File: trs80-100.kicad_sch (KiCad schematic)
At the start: 364 parts, among them CN2 A-7224, CN3 TCS-4480, CN4 TCS-4490, CN5 PRINTER CONNECTOR, CN6 RS232C, CN7 LCD-CONN, CN8 LCD-LED-CONN, J1 Adapter Jack CN9, K1 Key_Board, M1 40H373, M10 SystemBus, M11 ROM32k, M12 ROM32k, M13 40H032, M14 40H175, M15 40H244, M16 40H138, M17 40H000, M18 μPD1990AC, M19 80C85, M2 40H245, M20 40H367, M21 40H244, M22 IM6402, M23 40H244, M24 40H032, M25 81C55, M26 40H002, M27 4011, M28 4013, M29 TL064, M3 40H138, M30 TL064, M31 MC14412, M32 40H244, M33 40H157, M34 4584, M35 4584, M36 4013, M4 40H138, M5 40H139, M6 OPTION RAM #3, M7 OPTION RAM #2, M8 OPTION RAM #1, M9 STANDARD RAM, SW3 SLB-22BP-03, SW4 Reset Switch, SW5 SSP32201, T1 2SA1115, T10 2SC2603, T11 2SC2603, T13 2SC2603, T14 2SC2603(E), T15 2SC2603(E), T16 2SC2603(E), T17 2SC2603(E), T18 2SC2603, T19 2SA1115, T2 2SC2603, T20 2SC2603, T21 2SC2603(E), T22 2SC2603(E), T23 2SC2603, T24 2SC2603, T25 2SC2603, T27 2SC2603, T28 2SA1115, T3 2SC2603, T5 2SC2603, T6 2SC2603, T7 2SC2603, T8 2SC2603, T9 2SC2603, X1 32.768kHz, X2 4.9152MHz, X3 1.0MHz

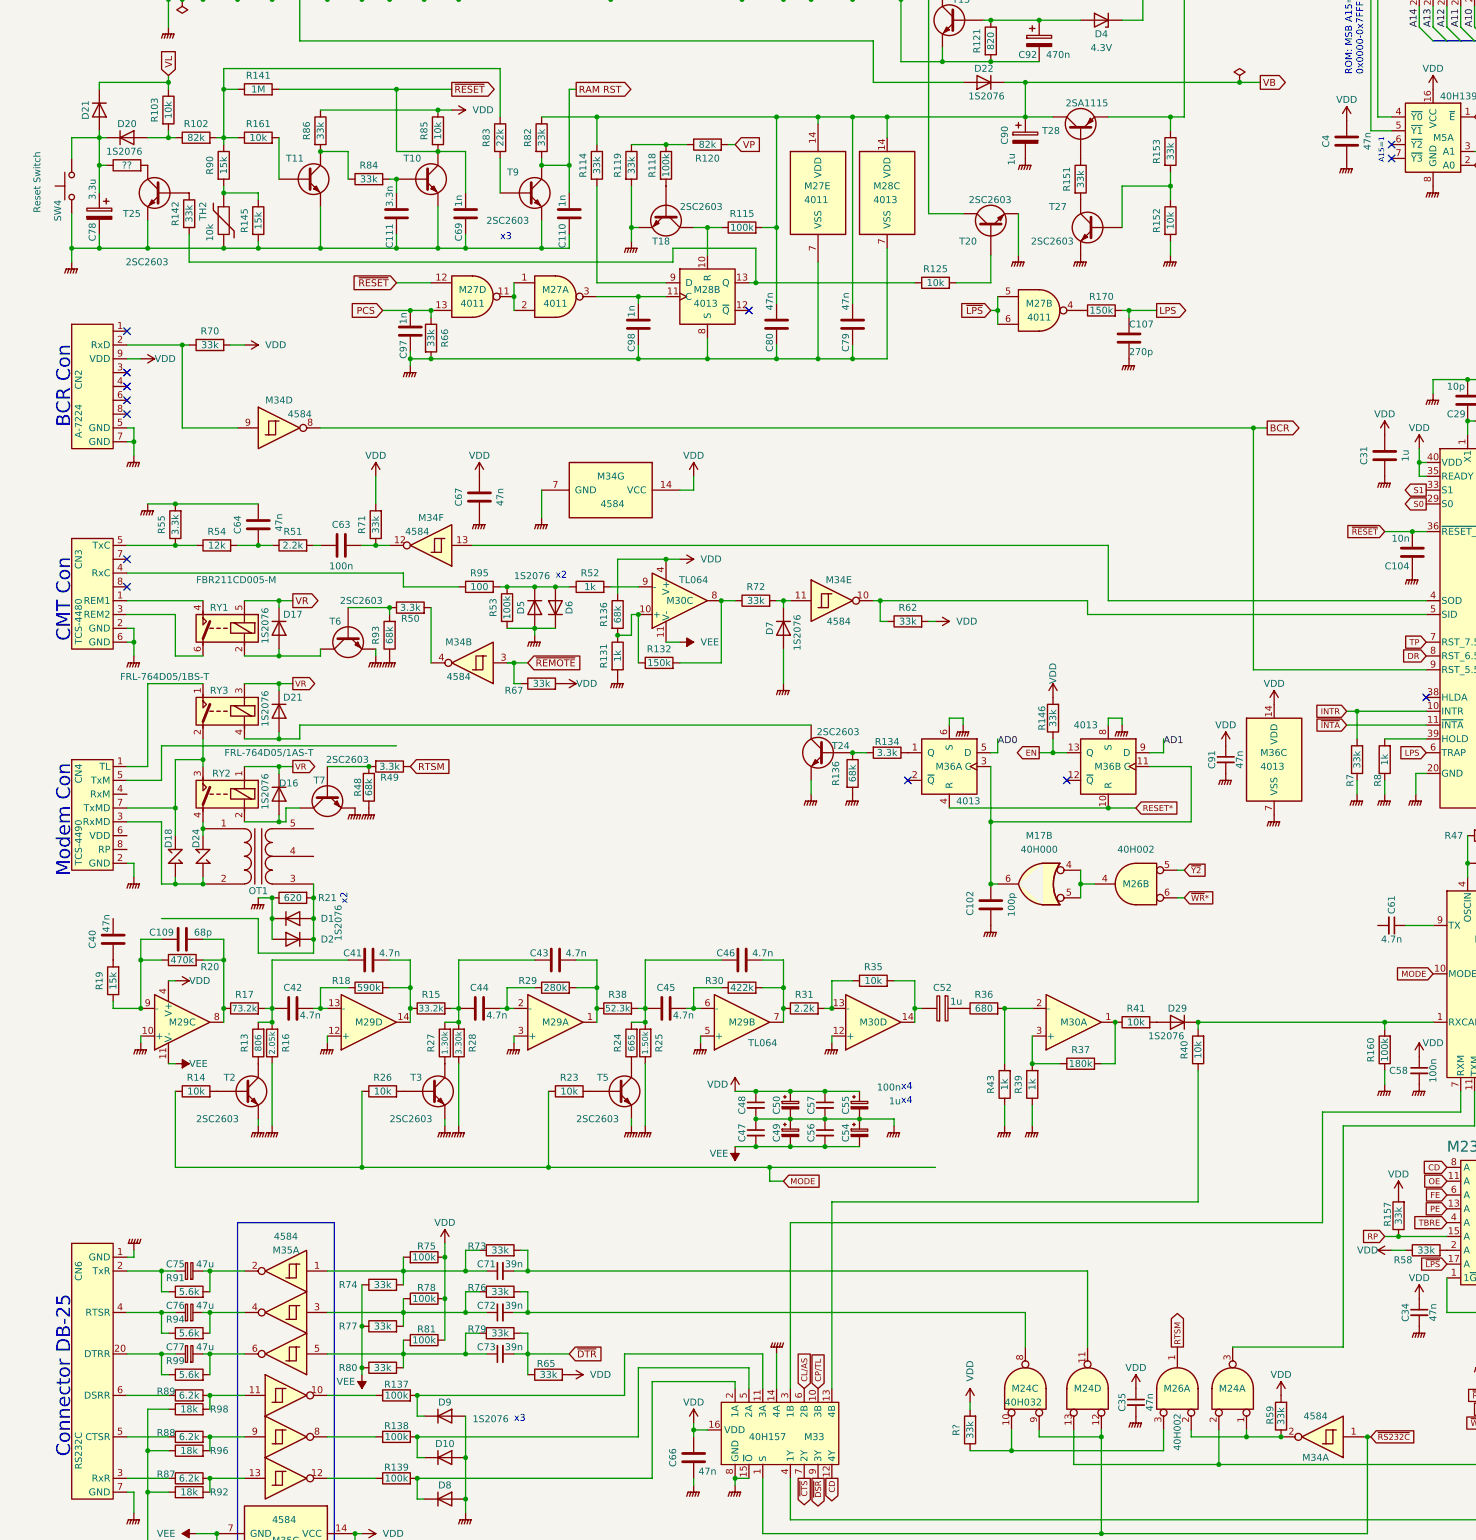
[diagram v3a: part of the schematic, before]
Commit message: Finish modem section.
Initial draft complete. One ERC warning about ~RTS never
used left.
Ready for proof-reading.
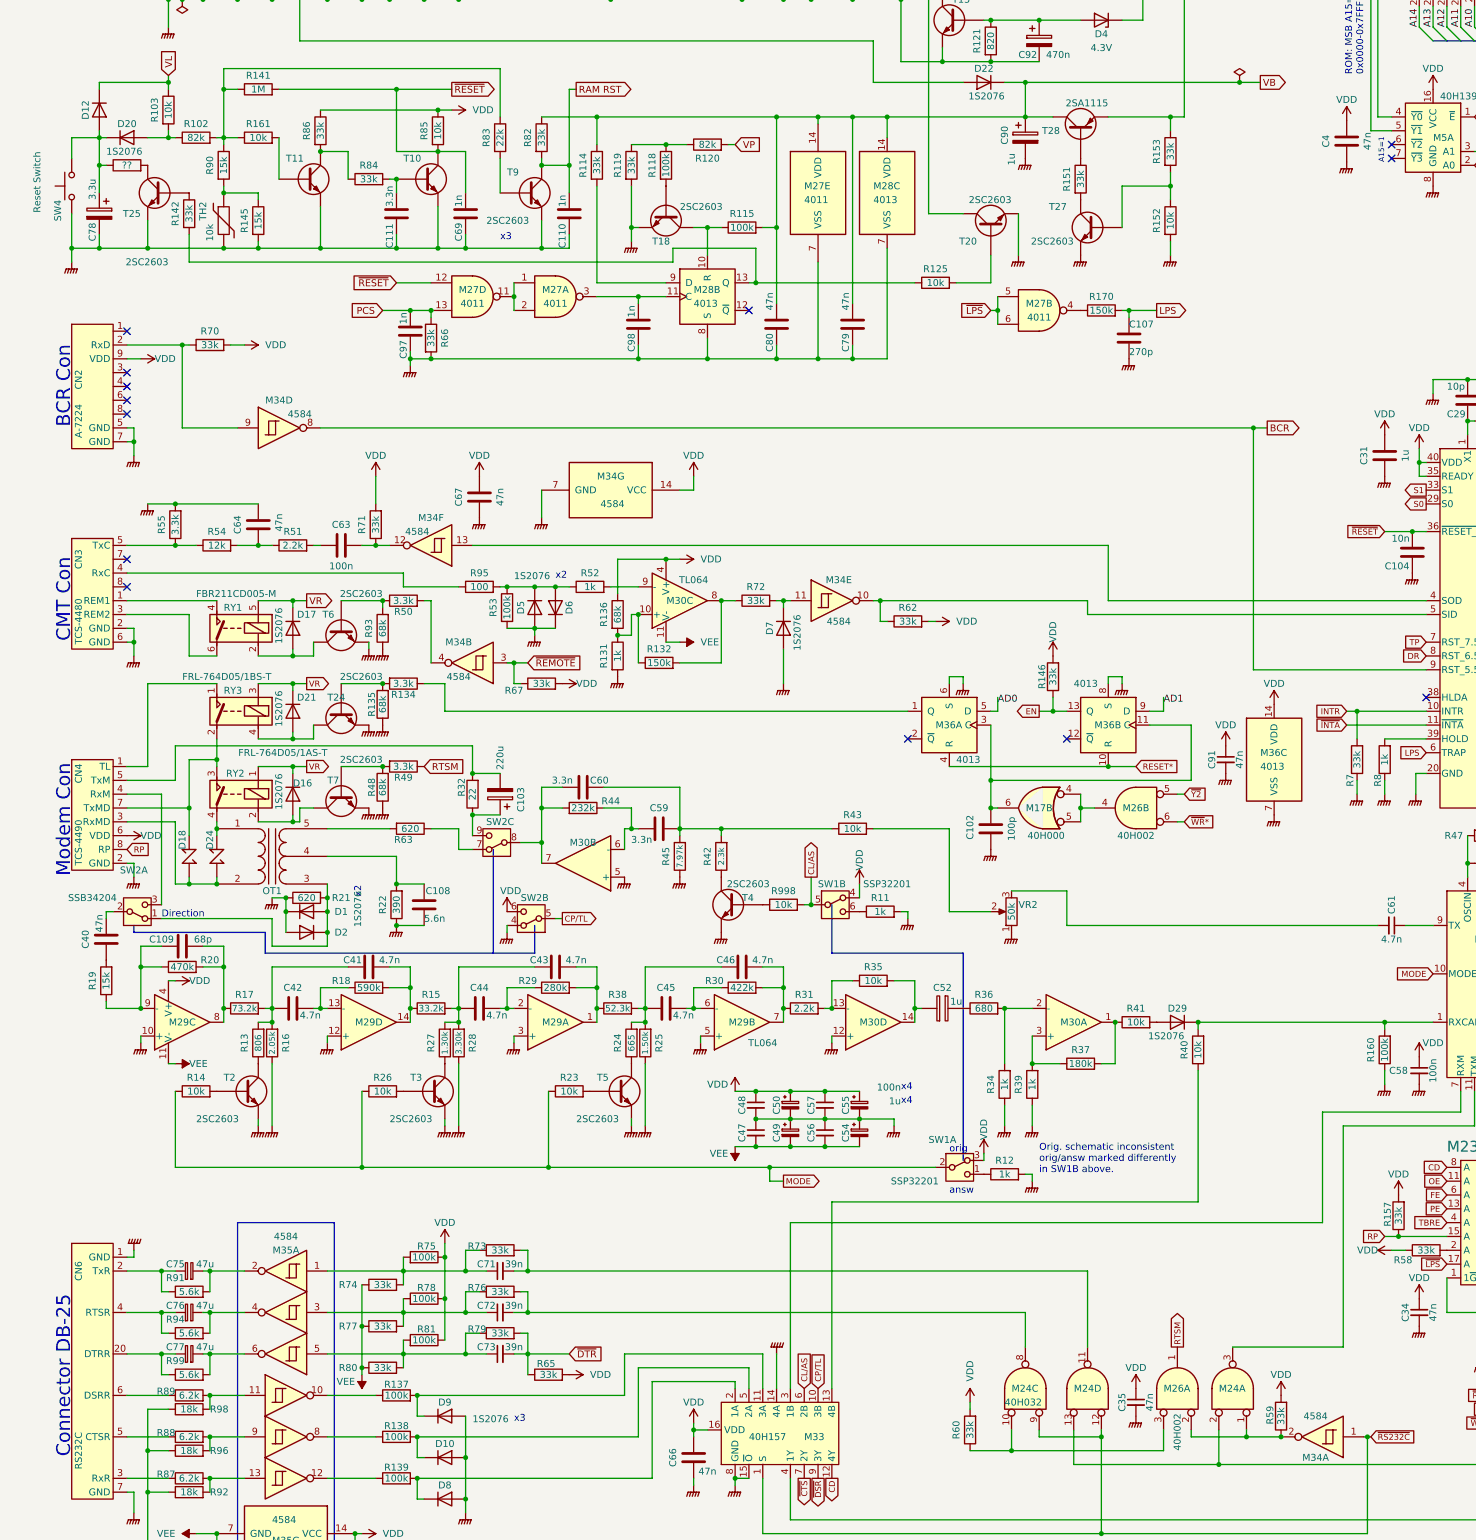
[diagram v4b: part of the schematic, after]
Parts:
- removed R136: 68k, symbol Device:R
- added C103: 220u, symbol Device:C_Polarized
- added C108: 5.6n, symbol Device:C
- added C59, C60: 3.3n, symbol Device:C
- added unit 2 of M30
- added R11, R12: 1k, symbol Device:R
- added R135: 68k, symbol Device:R
- added R22: 390, symbol Device:R
- added R32: 22, symbol Device:R
- added R42: 2.3k, symbol Device:R
- added R43, R998: 10k, symbol Device:R
- added R44: 232k, symbol Device:R
- added R45: 7.97k, symbol Device:R
- added R63: 620, symbol Device:R
- added SW1: SSP32201, symbol trs80-100:SW_SSP32201
- added SW2: SSB34204, symbol trs80-100:SW_SSB34204
- added T4: 2SC2603, Package_TO_SOT_THT:TO-92_Inline, symbol Transistor_BJT:2N3904
- added VR2: 50k, symbol Device:R_Potentiometer
- gave numbers to parts that had none: 1
- renumbered D21 to D12, R43 to R34
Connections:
- net CL/AS: now also R998.2, SW1.5 (B)
- net CP/TL: now also SW2.5 (B)
- net GNDPWR: now also C108.1, M30.5 (+), R11.2, R12.2, R135.1, R22.1, R45.1, SW2.4 (A), T4.1 (E), VR2.1
- net MODE: now also SW1.2 (B)
- net RP: now also CN4.8 (RP)
- net VDD: now also CN4.6 (VDD), SW1.3 (A), SW1.4 (A), SW2.6 (C)
- net at R134.2, T24.2 (B): now also R135.2
- net at C40.2: now also SW2.2 (B)
- net at CN4.4 (RxM): now also SW2.3 (C)
- net at CN4.5 (TxM): now also C103.2, R32.2
- net at D1.2 (A), D2.1 (K), OT1.3 (SA)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: now also SW2.1 (A)
- net at C61.2: now also VR2.3
- net at OT1.4 (SC): now also C108.2, R22.2
- net at OT1.5 (SB): now also R63.2
- new net: R998.1, T4.2 (B)
- new net: C59.1, C60.1, R42.2, R43.1, R45.2
- new net: C59.2, M30.6 (-), R44.1
- new net: R63.1, SW2.7 (A)
- new net: R43.2, VR2.2
- new net: C103.1, R32.1, SW2.9 (C)
- new net: R12.1, SW1.1 (C)
- new net: C60.2, M30.7, R44.2, SW2.8 (B)
- new net: R11.1, SW1.6 (C)
- new net: R42.1, T4.3 (C)
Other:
- note added: "Direction"
- note added: "Orig. schematic inconsistent orig/answ marked differently in SW1B above."
- note added: "answ"
- note added: "orig"
- moved on the sheet: C102, C109, C40, C41, C43, C46, D1, D16, D17, D18, D2, D21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

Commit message: Update README and manually fix broken symbol name for relay.
The '/' inside the symbol name for the relay was not making KiCAD
happy.
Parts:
- added C16: 47n, symbol Device:C_Small
- added C37: 100n, symbol Device:C_Small
- added R10: 1k, symbol Device:R
- D18, D24: value surge-absorber -> ERZ-C10DK361
- RY2: symbol trs80-100:FRL-764D05/1AS-T -> trs80-100:FRL-764D05_1AS-T
- RY3: symbol trs80-100:FRL-764D05/1BS-T -> trs80-100:FRL-764D05_1BS-T
- renumbered C999 to C62
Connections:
- net GNDPWR: now also C16.2, C37.1
- net VDD: now also C16.1, C37.2, R10.2; no longer SW2.6 (C)
- net ~{RTS}: now also M24.10, M26.3, R60.1
- new net: R10.1, SW2.6 (C)
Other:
- note added: "C37: BOM says 100n, schematic 47n. Former more plausible: big chip."
- note added: "Deduced from missing in BOM"
- note added: "R10? (1k)"
- note added: "R33 ?"
- moved on the sheet: C103, C108, C35, C39, C59, C60, D1, D2, M30B, R11, R21, R22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

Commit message: Free center part along the 'fold line' to not contain important components.
Fully printed, this is a A2 sheet. It is likely to be folded at least once,
so make sure only a few wires cross between the 'analog' and 'digital'
part of the circuit.
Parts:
- R162: renamed from R999; value ?? -> 100
- renumbered R998 to R33
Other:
- note added: "<- avoid components on fold line ->"
- note removed: "R10? (1k)"
- note removed: "R33 ?"
- moved on the sheet: BT1, BT2, C1, C10, C100, C101, C102, C103, C104, C105, C106, C107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
